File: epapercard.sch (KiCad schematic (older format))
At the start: 48 parts, among them P1 CONN_01X06, P2 A120699CT, Q1 2N7002KW, Q2 BSS84W, Q3 BSS84W, Q4 BSS84W, Q5 2N7002KW, Q6 2N7002KW, Q7 2N7002KW, SW1 SW_PUSH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

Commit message: Everything connected
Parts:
- U2: footprint TO_SOT_Packages_SMD:SOT-23-6_Handsoldering -> TO_SOT_Packages_SMD:SOT-23-6
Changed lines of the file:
@@
 Connection ~ 1450 3600
 $Comp
-L GND #PWR017
+L GND #PWR016
 U 1 1 5734F778
 P 1850 3950
-F 0 "#PWR017" H 1850 3700 50  0001 C CNN
+F 0 "#PWR016" H 1850 3700 50  0001 C CNN
 F 1 "GND" H 1850 3800 50  0000 C CNN
 F 2 "" H 1850 3950 50  0000 C CNN
@@
 Connection ~ 2400 3250
 $Comp
-L GND #PWR018
+L GND #PWR017
 U 1 1 5735025D
 P 2550 3750
-F 0 "#PWR018" H 2550 3500 50  0001 C CNN
+F 0 "#PWR017" H 2550 3500 50  0001 C CNN
 F 1 "GND" H 2550 3600 50  0000 C CNN
 F 2 "" H 2550 3750 50  0000 C CNN
@@
 Connection ~ 4450 2900
 $Comp
-L GND #PWR019
+L GND #PWR018
 U 1 1 57350E2E
 P 4000 3350
-F 0 "#PWR019" H 4000 3100 50  0001 C CNN
+F 0 "#PWR018" H 4000 3100 50  0001 C CNN
 F 1 "GND" H 4000 3200 50  0000 C CNN
 F 2 "" H 4000 3350 50  0000 C CNN
@@
 $EndComp
 $Comp
-L GND #PWR020
+L GND #PWR019
 U 1 1 57350EA2
 P 4450 3350
-F 0 "#PWR020" H 4450 3100 50  0001 C CNN
+F 0 "#PWR019" H 4450 3100 50  0001 C CNN
 F 1 "GND" H 4450 3200 50  0000 C CNN
 F 2 "" H 4450 3350 50  0000 C CNN
@@
 	4450 3350 4450 3250
 $Comp
-L +3.3VP #PWR021
+L +3.3VP #PWR020
 U 1 1 57351212
 P 4900 2900
-F 0 "#PWR021" H 5050 2850 50  0001 C CNN
+F 0 "#PWR020" H 5050 2850 50  0001 C CNN
 F 1 "+3.3VP" H 4900 3000 50  0000 C CNN
 F 2 "" H 4900 2900 50  0000 C CNN
@@
 $EndComp
 $Comp
-L GND #PWR022
+L GND #PWR021
 U 1 1 57353B9A
 P 6400 4900
-F 0 "#PWR022" H 6400 4650 50  0001 C CNN
+F 0 "#PWR021" H 6400 4650 50  0001 C CNN
 F 1 "GND" H 6400 4750 50  0000 C CNN
 F 2 "" H 6400 4900 50  0000 C CNN
@@
 button
 $Comp
-L GND #PWR023
+L GND #PWR022
 U 1 1 5735258C
 P 1850 5050
-F 0 "#PWR023" H 1850 4800 50  0001 C CNN
+F 0 "#PWR022" H 1850 4800 50  0001 C CNN
 F 1 "GND" H 1850 4900 50  0000 C CNN
 F 2 "" H 1850 5050 50  0000 C CNN
@@
 $EndComp
 $Comp
-L GND #PWR024
+L GND #PWR023
 U 1 1 5735319E
 P 3500 4600
-F 0 "#PWR024" H 3500 4350 50  0001 C CNN
+F 0 "#PWR023" H 3500 4350 50  0001 C CNN
 F 1 "GND" H 3500 4450 50  0000 C CNN
 F 2 "" H 3500 4600 50  0000 C CNN
@@
 led
 $Comp
-L GND #PWR025
+L GND #PWR024
 U 1 1 57353A35
 P 6350 1600
-F 0 "#PWR025" H 6350 1350 50  0001 C CNN
+F 0 "#PWR024" H 6350 1350 50  0001 C CNN
 F 1 "GND" H 6350 1450 50  0000 C CNN
 F 2 "" H 6350 1600 50  0000 C CNN
@@
 $EndComp
 $Comp
-L +3.3V #PWR026
+L +3.3V #PWR025
 U 1 1 57353E16
 P 6350 1100
-F 0 "#PWR026" H 6350 950 50  0001 C CNN
+F 0 "#PWR025" H 6350 950 50  0001 C CNN
 F 1 "+3.3V" H 6350 1240 50  0000 C CNN
 F 2 "" H 6350 1100 50  0000 C CNN
@@
 $EndComp
 $Comp
-L GND #PWR027
+L GND #PWR026
 U 1 1 57354BED
 P 6550 2850
-F 0 "#PWR027" H 6550 2600 50  0001 C CNN
+F 0 "#PWR026" H 6550 2600 50  0001 C CNN
 F 1 "GND" H 6550 2700 50  0000 C CNN
 F 2 "" H 6550 2850 50  0000 C CNN
@@
 	6550 2800 6650 2800
 $Comp
-L +3.3V #PWR028
+L +3.3V #PWR027
 U 1 1 57354DC5
 P 6550 2250
-F 0 "#PWR028" H 6550 2100 50  0001 C CNN
+F 0 "#PWR027" H 6550 2100 50  0001 C CNN
 F 1 "+3.3V" H 6550 2390 50  0000 C CNN
 F 2 "" H 6550 2250 50  0000 C CNN
@@
 $EndComp
 $Comp
-L +3.3V #PWR029
+L +3.3V #PWR028
 U 1 1 57357D99
 P 5350 2500
-F 0 "#PWR029" H 5350 2350 50  0001 C CNN
+F 0 "#PWR028" H 5350 2350 50  0001 C CNN
 F 1 "+3.3V" H 5350 2640 50  0000 C CNN
 F 2 "" H 5350 2500 50  0000 C CNN
@@
 Connection ~ 1550 800
 $Comp
-L GND #PWR030
+L GND #PWR029
 U 1 1 57358EA6
 P 1250 1150
-F 0 "#PWR030" H 1250 900 50  0001 C CNN
+F 0 "#PWR029" H 1250 900 50  0001 C CNN
 F 1 "GND" H 1250 1000 50  0000 C CNN
 F 2 "" H 1250 1150 50  0000 C CNN
@@
 F 0 "U2" H 2450 6550 50  0000 C CNN
 F 1 "TLV61225" H 2450 6750 50  0000 C CNN
-F 2 "TO_SOT_Packages_SMD:SOT-23-6_Handsoldering" H 2450 6650 50  0001 C CNN
+F 2 "TO_SOT_Packages_SMD:SOT-23-6" H 2450 6650 50  0001 C CNN
 F 3 "DOCUMENTATION" H 2450 6650 50  0001 C CNN
 	1    2450 6650
@@
 $EndComp
 $Comp
-L +3.3V #PWR031
+L +3.3V #PWR030
 U 1 1 577DEF3F
 P 750 6450
-F 0 "#PWR031" H 750 6300 50  0001 C CNN
+F 0 "#PWR030" H 750 6300 50  0001 C CNN
 F 1 "+3.3V" H 750 6590 50  0000 C CNN
 F 2 "" H 750 6450 50  0000 C CNN
@@
 	750  6550 1500 6550
 $Comp
-L GND #PWR032
+L GND #PWR031
 U 1 1 577DF43A
 P 1250 6900
-F 0 "#PWR032" H 1250 6650 50  0001 C CNN
+F 0 "#PWR031" H 1250 6650 50  0001 C CNN
 F 1 "GND" H 1250 6750 50  0000 C CNN
 F 2 "" H 1250 6900 50  0000 C CNN
@@
 Connection ~ 4350 6550
 $Comp
-L GND #PWR033
+L GND #PWR032
 U 1 1 577E2C3D
 P 4350 7050
-F 0 "#PWR033" H 4350 6800 50  0001 C CNN
+F 0 "#PWR032" H 4350 6800 50  0001 C CNN
 F 1 "GND" H 4350 6900 50  0000 C CNN
 F 2 "" H 4350 7050 50  0000 C CNN
@@
 $EndComp
 $Comp
-L GND #PWR034
+L GND #PWR033
 U 1 1 577E2D8A
 P 850 7050
-F 0 "#PWR034" H 850 6800 50  0001 C CNN
+F 0 "#PWR033" H 850 6800 50  0001 C CNN
 F 1 "GND" H 850 6900 50  0000 C CNN
 F 2 "" H 850 7050 50  0000 C CNN

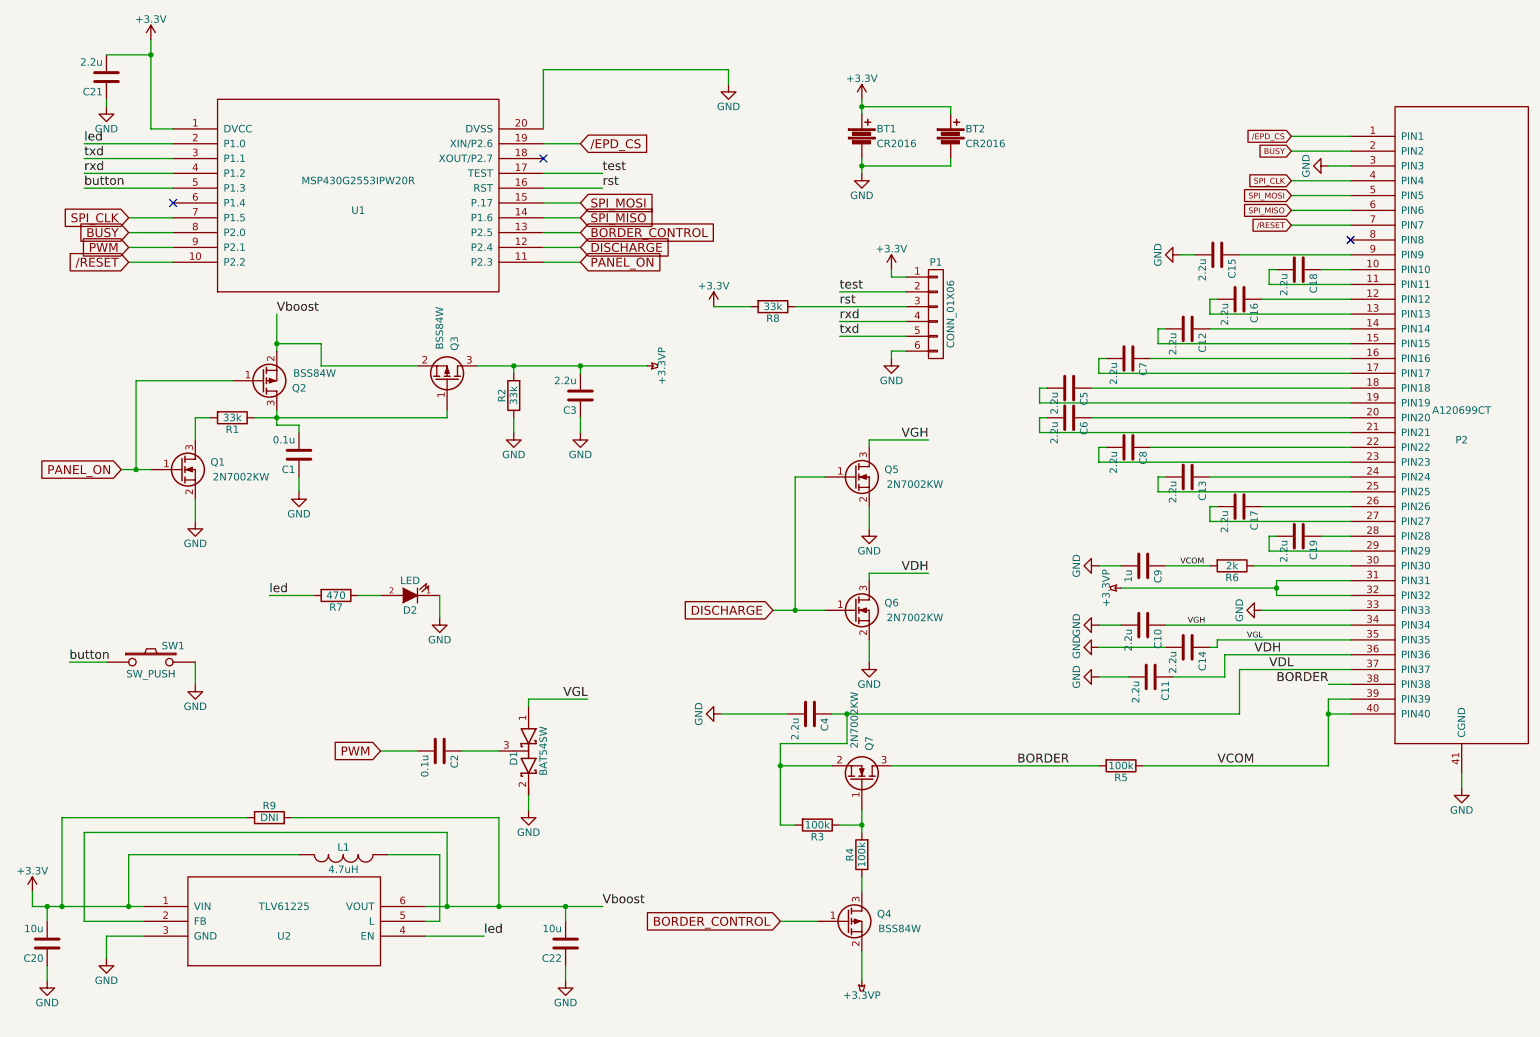
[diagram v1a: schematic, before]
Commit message: Fixed TLV61225 footprint
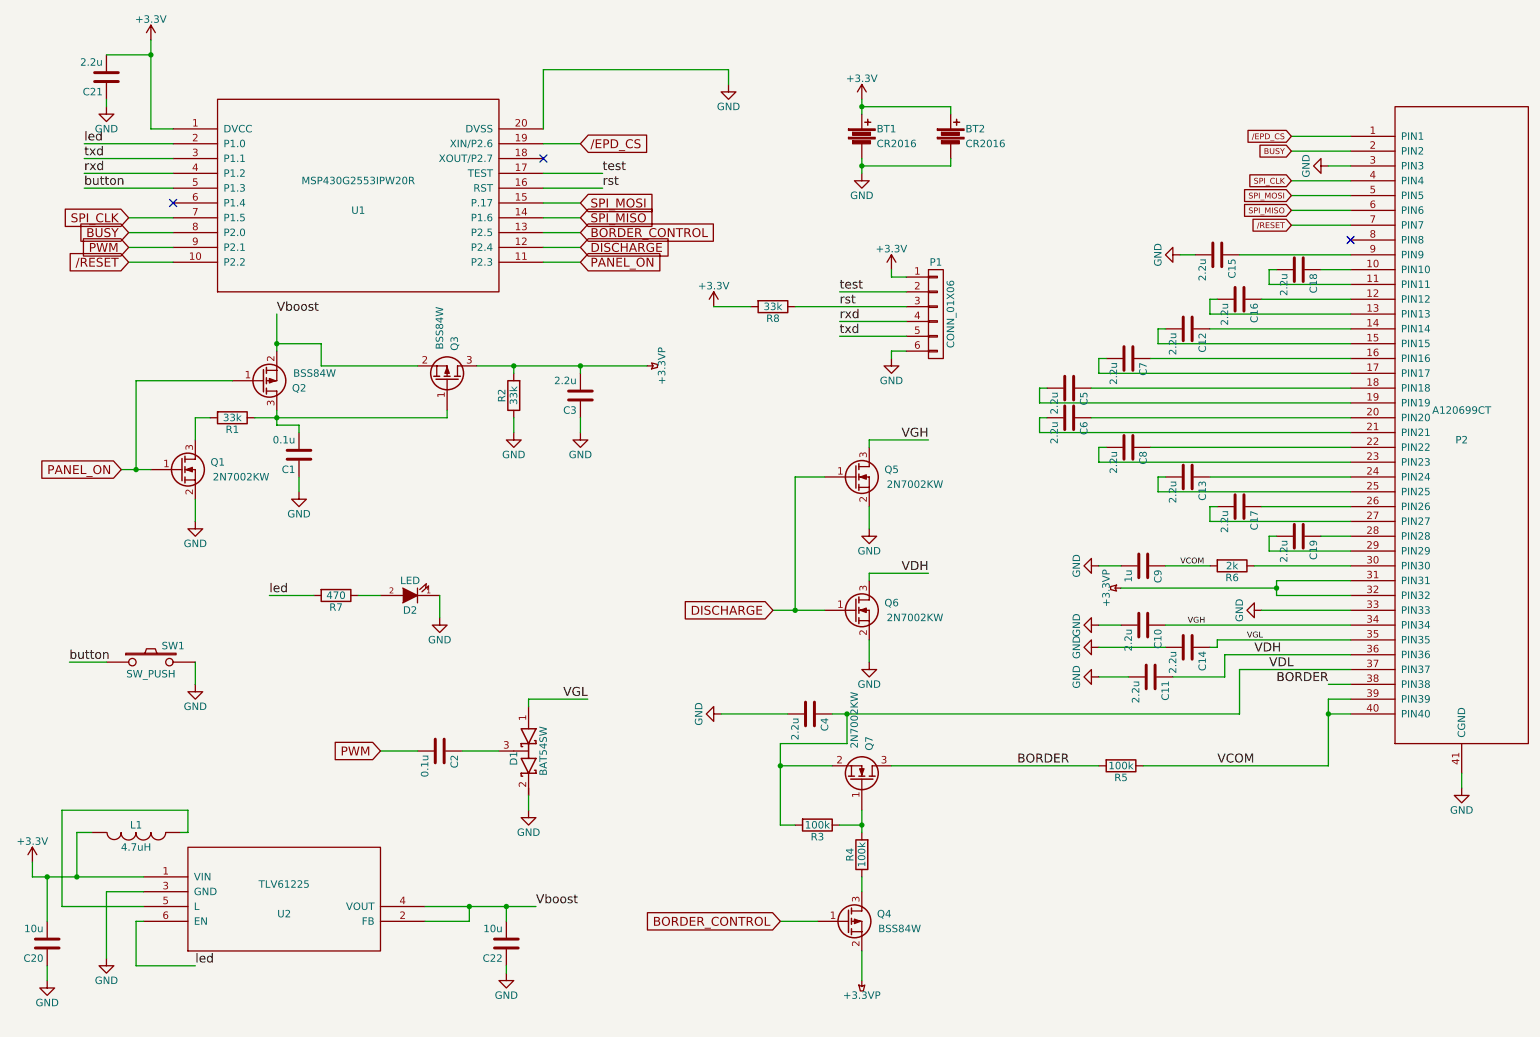
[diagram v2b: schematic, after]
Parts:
- removed R9: DNI, Resistors_SMD:R_0201, symbol R
- removed U2: TLV61225, TO_SOT_Packages_SMD:SOT-23-6, symbol TLV61224
- added U2: TLV61225, TO_SOT_Packages_SMD:SOT-23-6, symbol TLV61225
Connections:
- net +3V3: now also U2.1 (VIN)
- net GND: now also U2.3 (GND)
- net Vboost: now also U2.2 (FB), U2.4 (VOUT)
- net led: now also U2.6 (EN)
- net at L1.2: now also U2.5 (L)
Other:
- moved on the sheet: C22, L1

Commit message: Fixed boost regulator
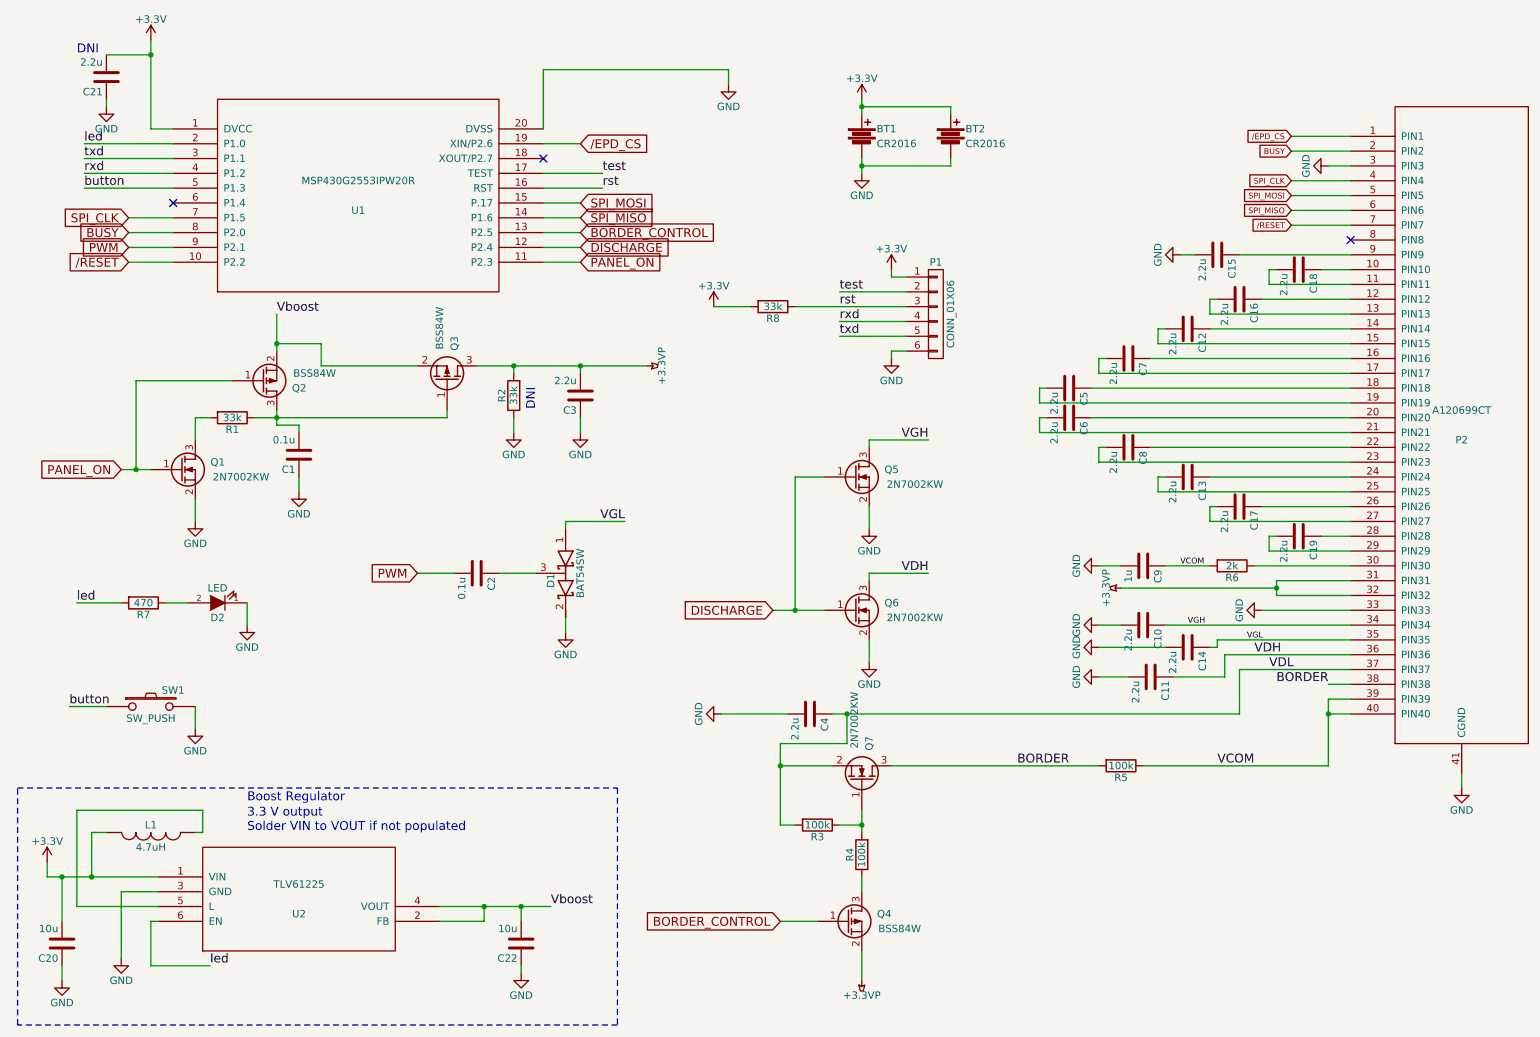
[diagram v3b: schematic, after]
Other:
- note added: "3.3 V output\nSolder VIN to VOUT if not populated"
- note added: "Boost Regulator"
- note added: "DNI"
- moved on the sheet: C2, C20, C22, D1, D2, L1, R7, SW1, U2
